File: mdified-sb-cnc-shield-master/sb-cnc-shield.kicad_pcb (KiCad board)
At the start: 2 copper layers, 68.6 x 53.3 mm, 62 parts, among them P1 XMOT, P2 YMOT, P3 ZMOT, P4 AMOT, P5 UART, P6 I2C, P7 ES_SETUP, P8 12V-36V, SW1 RESET, U1 ARDUINO_UNO_SHIELD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

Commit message: modify name
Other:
- board text added: "PnPduino v1"
- board text removed: "SB CNC SHIELD"
- board text removed: "www.staticboards.com"
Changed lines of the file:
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@@
   (general
     (thickness 1.6)
-    (drawings 40)
+    (drawings 39)
     (tracks 846)
     (zones 0)
@@
     (effects (font (size 0.8 0.8) (thickness 0.125)))
   )
-  (gr_text www.staticboards.com (at 139.573 117.221) (layer F.SilkS)
-    (effects (font (size 0.8 0.8) (thickness 0.2)))
-  )
   (gr_text EN (at 153.8605 71.882) (layer F.SilkS)
     (effects (font (size 1.5 1.5) (thickness 0.3)))
@@
     (arrow2b (pts (xy 182.88 60.960001) (xy 181.753496 61.546422)))
   )
-  (gr_text "SB CNC SHIELD" (at 139.446 115.824) (layer F.SilkS)
+  (gr_text "PnPduino v1" (at 138.60272 116.2304) (layer F.SilkS)
     (effects (font (size 1 1) (thickness 0.25)))
   )
@@
   (segment (start 144.145 109.855) (end 142.91564 111.08436) (width 0.45) (layer F.Cu) (net 22))
   (segment (start 141.01572 111.08436) (end 140.83792 110.90656) (width 0.45) (layer F.Cu) (net 22))
-  (segment (start 139.484921 109.719559) (end 138.29792 110.90656) (width 0.45) (layer B.Cu) (net 22))
-  (segment (start 139.484921 107.796799) (end 139.484921 109.719559) (width 0.45) (layer B.Cu) (net 22))
-  (segment (start 139.065 103.378) (end 139.065 107.376878) (width 0.45) (layer B.Cu) (net 22))
-  (segment (start 137.033 101.346) (end 139.065 103.378) (width 0.45) (layer B.Cu) (net 22))
-  (segment (start 137.033 91.567) (end 137.033 101.346) (width 0.45) (layer B.Cu) (net 22))
-  (segment (start 139.065 107.376878) (end 139.484921 107.796799) (width 0.45) (layer B.Cu) (net 22))
-  (segment (start 137.83056 90.76944) (end 137.033 91.567) (width 0.45) (layer B.Cu) (net 22))
   (segment (start 140.90904 111.08436) (end 140.70076 111.29264) (width 0.45) (layer F.Cu) (net 22))
   (segment (start 142.91564 111.08436) (end 140.90904 111.08436) (width 0.45) (layer F.Cu) (net 22))
   (segment (start 138.16076 111.29264) (end 140.70076 111.29264) (width 0.45) (layer F.Cu) (net 22))
   (segment (start 135.62076 111.29264) (end 138.16076 111.29264) (width 0.45) (layer F.Cu) (net 22))
+  (segment (start 139.484921 109.968479) (end 138.16076 111.29264) (width 0.45) (layer B.Cu) (net 22))
+  (segment (start 139.065 103.378) (end 139.065 107.376878) (width 0.45) (layer B.Cu) (net 22))
+  (segment (start 137.033 101.346) (end 139.065 103.378) (width 0.45) (layer B.Cu) (net 22))
+  (segment (start 139.484921 107.796799) (end 139.484921 109.968479) (width 0.45) (layer B.Cu) (net 22))
+  (segment (start 139.065 107.376878) (end 139.484921 107.796799) (width 0.45) (layer B.Cu) (net 22))
+  (segment (start 137.033 91.567) (end 137.033 101.346) (width 0.45) (layer B.Cu) (net 22))
+  (segment (start 137.83056 90.76944) (end 137.033 91.567) (width 0.45) (layer B.Cu) (net 22))
   (segment (start 131.445 76.835) (end 132.512731 76.835) (width 0.25) (layer F.Cu) (net 23))
   (segment (start 133.985 76.835) (end 133.985 75.88) (width 0.25) (layer F.Cu) (net 23))

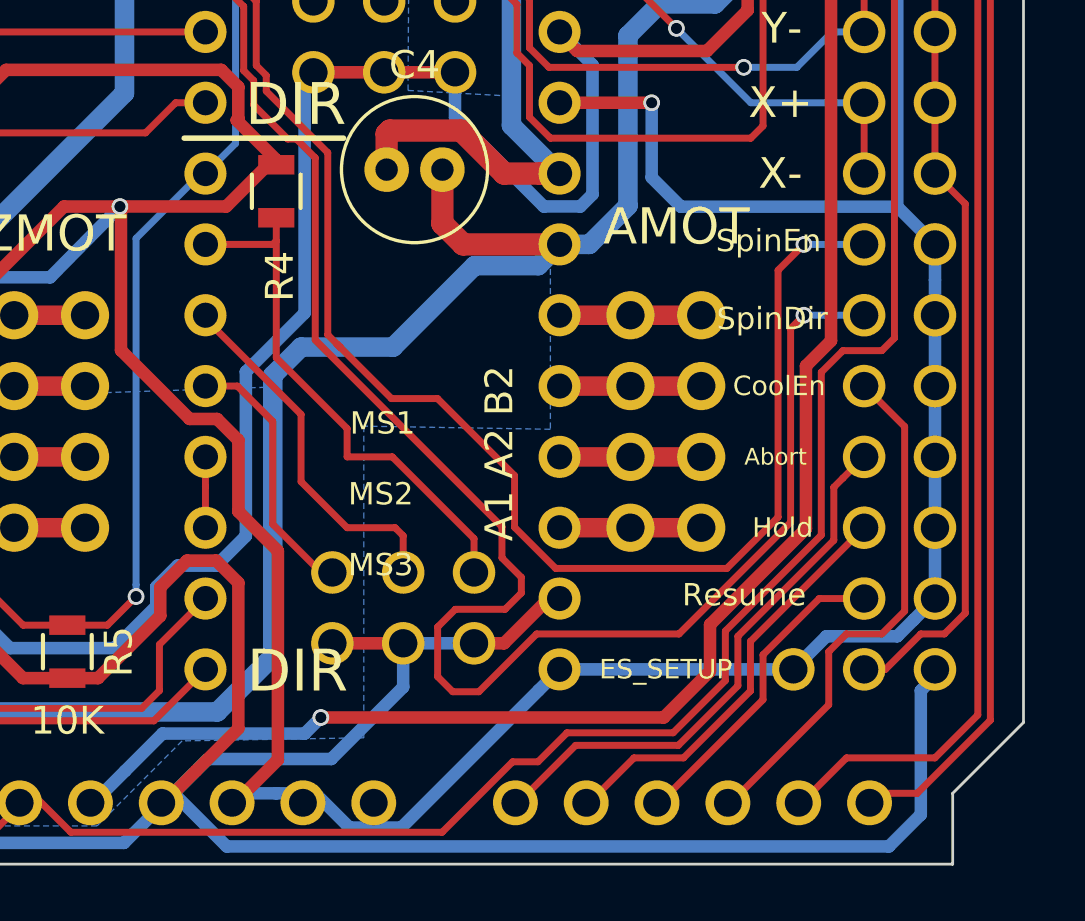
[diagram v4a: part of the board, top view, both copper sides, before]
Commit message: connect GNDs and connect the e-stop for reset
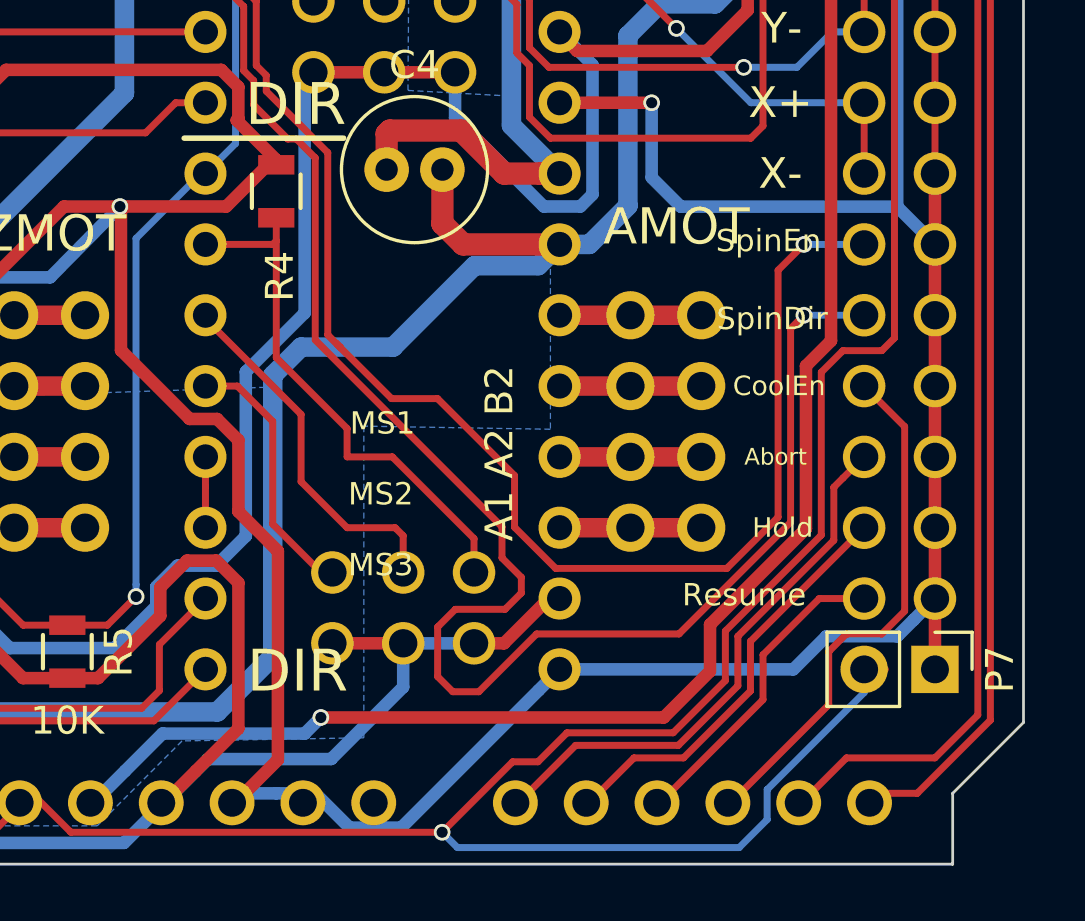
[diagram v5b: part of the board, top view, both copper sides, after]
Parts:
- P7: value ES_SETUP -> E-STOP; footprint Pin_Headers:Pin_Header_Straight_1x03 -> Connector_PinHeader_2.54mm:PinHeader_1x02_P2.54mm_Vertical
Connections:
- JP13 pad 1: EN_SETUP -> GND
- JP14 pad 1: EN_SETUP -> GND
- JP15 pad 1: EN_SETUP -> GND
- JP16 pad 1: EN_SETUP -> GND
- JP17 pad 1: EN_SETUP -> GND
- JP18 pad 1: EN_SETUP -> GND
- P7 pad 1: +5V -> GND
- P7 pad 2: EN_SETUP -> RESET
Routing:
- net +5V: track 259.8 -> 226.4 mm
- net EN_SETUP: track 33.4 -> 0.00 mm
- net RESET: track 151.5 -> 171.4 mm, vias 0 -> 1
- net GND: track 274.2 -> 292.2 mm
